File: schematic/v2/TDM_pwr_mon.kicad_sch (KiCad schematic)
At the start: 42 parts, among them J10 INA219_CONFIG, J11 INA219_CONFIG, J15 INA219_CONFIG, J5 INA219_CONFIG, J6 INA219_CONFIG, J7 INA219_CONFIG, U10 INA219AxD, U11 INA219AxD, U12 INA219AxD, U13 INA219AxD, U20 INA219AxD, U7 INA219AxD

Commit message: no errors in the ERC!
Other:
- note added: "PMS has an INA219 current sensor for each board/node in on the PCB. Each takes in the 5V from it's parent board and supplies 5V to said board's circuit (its peripherals) thus enabling monitoring"
- note added: "Power Monitor and Supply"
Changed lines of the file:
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@@
 		)
 	)
+	(text "PMS has an INA219 current sensor\nfor each board/node in on the \nPCB. Each takes in the 5V from it's\nparent board and supplies 5V to said\nboard's circuit (its peripherals)\nthus enabling monitoring"
+		(exclude_from_sim no)
+		(at 34.29 32.512 0)
+		(effects
+			(font
+				(size 1.27 1.27)
+			)
+		)
+	)
 	(text "INA219 ACM"
 		(exclude_from_sim no)
@@
 		)
 	)
+	(text "Power Monitor and Supply"
+		(exclude_from_sim no)
+		(at 16.51 23.114 0)
+		(effects
+			(font
+				(size 5.9944 5.9944)
+				(thickness 1.1989)
+				(bold yes)
+			)
+			(justify left bottom)
+		)
+	)
 	(text "INA219 UUM"
 		(exclude_from_sim no)
@@
 	)
 	(junction
+		(at 156.21 48.26)
+		(diameter 0)
+		(color 0 0 0 0)
+	)
+	(junction
 		(at 186.69 93.98)
 		(diameter 0)
@@
 	(wire
 		(pts
-			(xy 153.67 48.26) (xy 157.48 48.26)
+			(xy 167.64 38.1) (xy 167.64 40.64)
+		)
+		(stroke
+			(width 0)
+			(type default)
+		)
+	)
+	(wire
+		(pts
+			(xy 153.67 48.26) (xy 156.21 48.26)
 		)
 		(stroke
@@
 	(wire
 		(pts
-			(xy 163.83 78.74) (xy 167.64 78.74)
+			(xy 156.21 48.26) (xy 157.48 48.26)
 		)
 		(stroke
@@
 	(wire
 		(pts
-			(xy 101.6 134.62) (xy 102.87 134.62)
+			(xy 157.48 132.08) (xy 157.48 134.62)
+		)
+		(stroke
+			(width 0)
+			(type default)
+		)
+	)
+	(wire
+		(pts
+			(xy 163.83 78.74) (xy 167.64 78.74)
 		)
 		(stroke
@@
 	(wire
 		(pts
+			(xy 102.87 132.08) (xy 102.87 134.62)
+		)
+		(stroke
+			(width 0)
+			(type default)
+		)
+	)
+	(wire
+		(pts
 			(xy 154.94 59.69) (xy 154.94 63.5)
 		)
@@
 	(wire
 		(pts
+			(xy 157.48 91.44) (xy 157.48 93.98)
+		)
+		(stroke
+			(width 0)
+			(type default)
+		)
+	)
+	(wire
+		(pts
 			(xy 100.33 63.5) (xy 102.87 63.5)
 		)
@@
 	(wire
 		(pts
-			(xy 156.21 53.34) (xy 157.48 53.34)
+			(xy 154.94 50.8) (xy 157.48 50.8)
 		)
 		(stroke
@@
 	(wire
 		(pts
-			(xy 167.64 118.11) (xy 167.64 119.38)
+			(xy 99.06 88.9) (xy 102.87 88.9)
 		)
 		(stroke
@@
 	(wire
 		(pts
-			(xy 177.8 137.16) (xy 179.07 137.16)
+			(xy 167.64 118.11) (xy 167.64 119.38)
 		)
 		(stroke
@@
 	(wire
 		(pts
-			(xy 113.03 101.6) (xy 113.03 102.87)
+			(xy 177.8 137.16) (xy 179.07 137.16)
 		)
 		(stroke
@@
 	(wire
 		(pts
-			(xy 123.19 96.52) (xy 124.46 96.52)
+			(xy 113.03 101.6) (xy 113.03 102.87)
 		)
 		(stroke
@@
 	(wire
 		(pts
-			(xy 153.67 88.9) (xy 157.48 88.9)
+			(xy 123.19 96.52) (xy 124.46 96.52)
 		)
 		(stroke
@@
 	(wire
 		(pts
-			(xy 167.64 38.1) (xy 167.64 40.64)
-		)
-		(stroke
-			(width 0)
-			(type default)
-		)
-	)
-	(wire
-		(pts
 			(xy 91.44 100.33) (xy 92.71 100.33)
 		)
@@
 	(wire
 		(pts
-			(xy 156.21 134.62) (xy 157.48 134.62)
+			(xy 154.94 132.08) (xy 157.48 132.08)
 		)
 		(stroke
@@
 	(wire
 		(pts
-			(xy 156.21 93.98) (xy 157.48 93.98)
+			(xy 154.94 91.44) (xy 157.48 91.44)
 		)
 		(stroke
@@
 	(wire
 		(pts
-			(xy 101.6 53.34) (xy 102.87 53.34)
+			(xy 100.33 50.8) (xy 102.87 50.8)
 		)
 		(stroke
@@
 	(wire
 		(pts
-			(xy 101.6 93.98) (xy 102.87 93.98)
+			(xy 100.33 91.44) (xy 101.6 91.44)
 		)
 		(stroke
@@
 	(wire
 		(pts
+			(xy 102.87 132.08) (xy 100.33 132.08)
+		)
+		(stroke
+			(width 0)
+			(type default)
+		)
+	)
+	(wire
+		(pts
 			(xy 186.69 53.34) (xy 190.5 53.34)
 		)
@@
 	(wire
 		(pts
+			(xy 102.87 50.8) (xy 102.87 53.34)
+		)
+		(stroke
+			(width 0)
+			(type default)
+		)
+	)
+	(wire
+		(pts
 			(xy 156.21 38.1) (xy 158.75 38.1)
 		)
@@
 	(wire
 		(pts
+			(xy 101.6 91.44) (xy 101.6 93.98)
+		)
+		(stroke
+			(width 0)
+			(type default)
+		)
+	)
+	(wire
+		(pts
 			(xy 91.44 140.97) (xy 92.71 140.97)
 		)
@@
 	(wire
 		(pts
+			(xy 101.6 93.98) (xy 102.87 93.98)
+		)
+		(stroke
+			(width 0)
+			(type default)
+		)
+	)
+	(wire
+		(pts
 			(xy 179.07 137.16) (xy 186.69 137.16)
 		)
@@
 	(wire
 		(pts
+			(xy 153.67 88.9) (xy 157.48 88.9)
+		)
+		(stroke
+			(width 0)
+			(type default)
+		)
+	)
+	(wire
+		(pts
 			(xy 91.44 59.69) (xy 92.71 59.69)
 		)
@@
 	(wire
 		(pts
-			(xy 99.06 88.9) (xy 102.87 88.9)
-		)
-		(stroke
-			(width 0)
-			(type default)
-		)
-	)
-	(wire
-		(pts
 			(xy 132.08 53.34) (xy 135.89 53.34)
 		)
@@
 	(wire
 		(pts
+			(xy 157.48 50.8) (xy 157.48 53.34)
+		)
+		(stroke
+			(width 0)
+			(type default)
+		)
+	)
+	(wire
+		(pts
 			(xy 157.48 137.16) (xy 157.48 134.62)
 		)
@@
 	(hierarchical_label "DSM_VDD"
 		(shape output)
-		(at 156.21 53.34 180)
+		(at 154.94 50.8 180)
 		(effects
 			(font
@@
 	(hierarchical_label "UUM_VDD"
 		(shape output)
-		(at 156.21 93.98 180)
+		(at 154.94 91.44 180)
 		(effects
 			(font
@@
 	(hierarchical_label "TDM_VDD"
 		(shape output)
-		(at 101.6 53.34 180)
+		(at 100.33 50.8 180)
 		(effects
 			(font
@@
 	(hierarchical_label "7SDD_VDD"
 		(shape output)
-		(at 156.21 134.62 180)
+		(at 154.94 132.08 180)
 		(effects
 			(font
@@
 	(hierarchical_label "APM_VDD"
 		(shape output)
-		(at 101.6 134.62 180)
+		(at 100.33 132.08 180)
 		(effects
 			(font
@@
 	(hierarchical_label "ACM_VDD"
 		(shape output)
-		(at 101.6 93.98 180)
+		(at 100.33 91.44 180)
 		(effects
 			(font
@@
 	)
 	(symbol
+		(lib_id "power:PWR_FLAG")
+		(at 156.21 48.26 0)
+		(unit 1)
+		(exclude_from_sim no)
+		(in_bom yes)
+		(on_board yes)
+		(dnp no)
+		(fields_autoplaced yes)
+		(property "Reference" "#FLG012"
+			(at 156.21 46.355 0)
+			(effects
+				(font
+					(size 1.27 1.27)
+				)
+				(hide yes)
+			)
+		)
+		(property "Value" "PWR_FLAG"
+			(at 156.21 43.18 0)
+			(effects
+				(font
+					(size 1.27 1.27)
+				)
+			)
+		)
+		(property "Footprint" ""
+			(at 156.21 48.26 0)
+			(effects
+				(font
+					(size 1.27 1.27)
+				)
+				(hide yes)
+			)
+		)
+		(property "Datasheet" "~"
+			(at 156.21 48.26 0)
+			(effects
+				(font
+					(size 1.27 1.27)
+				)
+				(hide yes)
+			)
+		)
+		(property "Description" "Special symbol for telling ERC where power comes from"
+			(at 156.21 48.26 0)
+			(effects
+				(font
+					(size 1.27 1.27)
+				)
+				(hide yes)
+			)
+		)
+		(pin "1"
+		)
+		(instances
+			(project ""
+				(path "/fe7b15e9-f0ed-4338-9f03-dd7651dace13/442c7b41-f8c0-48e5-8b80-63d502cac366/c9161959-85ce-4cf5-b3d5-3776fec616f5"
+					(reference "#FLG012")
+					(unit 1)
+				)
+			)
+		)
+	)
+	(symbol
 		(lib_id "power:+5V")
 		(at 113.03 77.47 0)
@@
 		(on_board yes)
 		(dnp no)
-		(fields_autoplaced yes)
 		(property "Reference" "#PWR050"
 			(at 153.67 52.07 0)
@@
 		)
 		(property "Value" "5V_DSM"
-			(at 156.21 46.9899 0)
+			(at 152.146 44.958 0)
 			(effects
 				(font

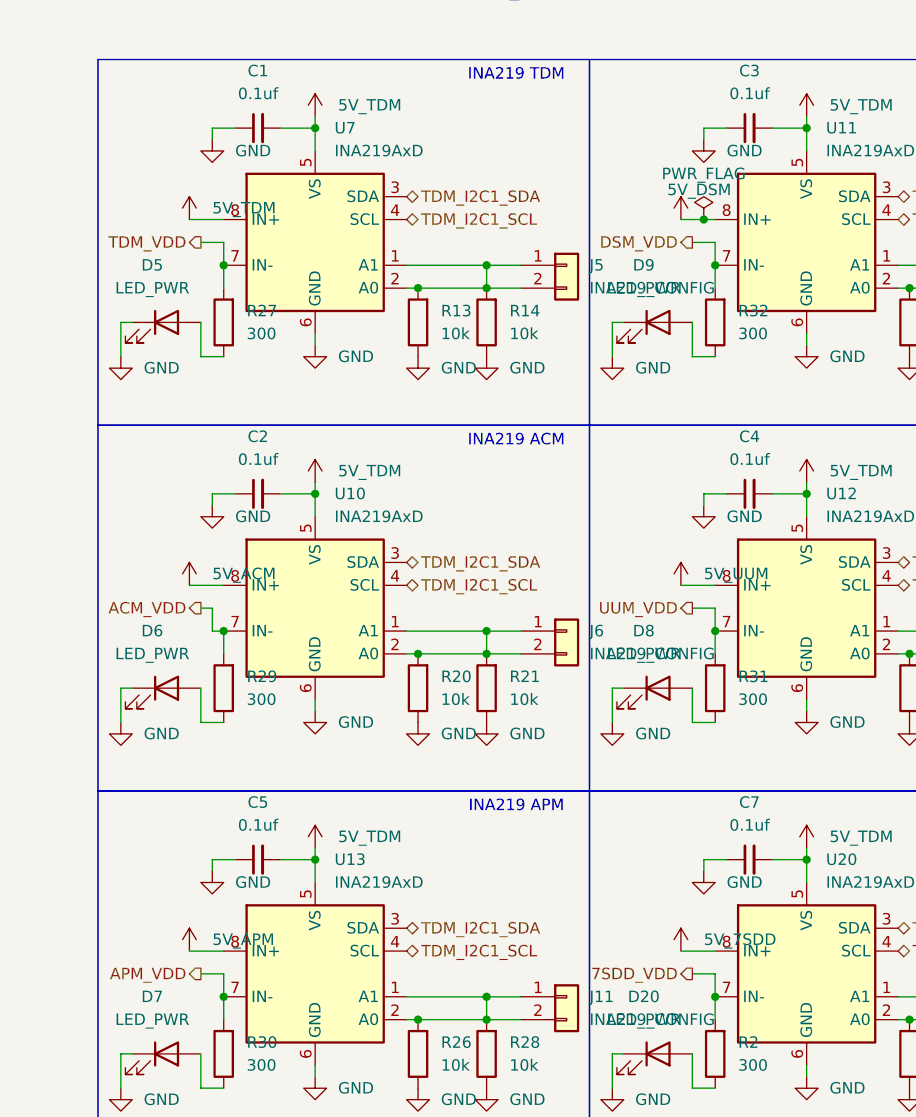
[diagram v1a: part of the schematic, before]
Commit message: schematic updates, no errors at least. running DRC on pcb
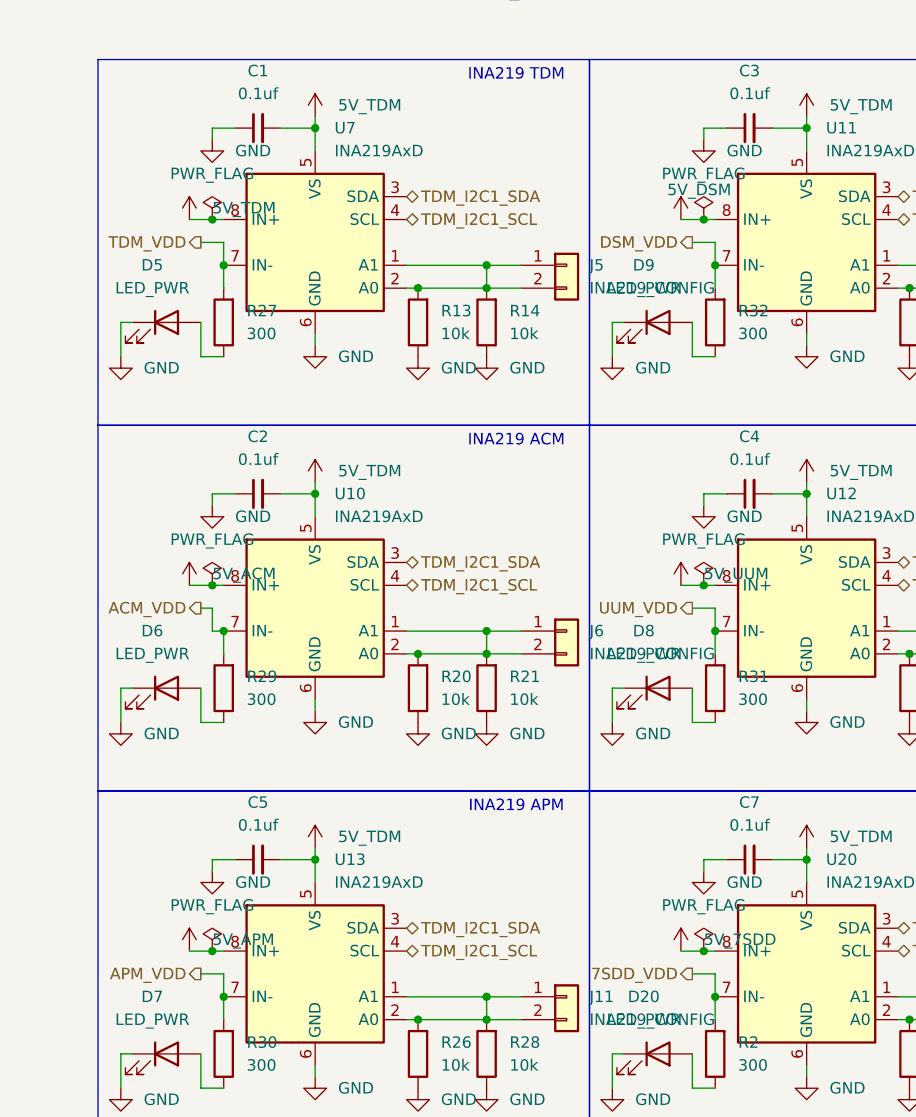
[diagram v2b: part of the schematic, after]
